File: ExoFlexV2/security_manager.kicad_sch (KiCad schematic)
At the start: 8 parts, among them U10 SN74HC7032D_V2, U6 SN74HC7032D_V2, U7 SN74HC7032D_V2, U8 SN74LV4T08PWR_V2, U9 SN74LV4T08PWR_V2

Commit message: quque truc
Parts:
- renumbered U9 to U10, U10 to U11, U6 to U7, U7 to U8, U8 to U9
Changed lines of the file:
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@@
   (symbol (lib_id "SymLib:SN74HC7032D_V2") (at 59.69 30.48 0) (unit 2)
     (in_bom yes) (on_board yes) (fields_autoplaced)
-    (property "Reference" "U6" (id 0) (at 59.69 21.59 0))
+    (property "Reference" "U7" (id 0) (at 59.69 21.59 0))
     (property "Value" "SN74HC7032D_V2" (id 1) (at 59.69 24.13 0))
     (property "Footprint" "FootPrint:SN74HC7032D" (id 2) (at 59.69 33.02 0)
@@
   (symbol (lib_id "SymLib:SN74HC7032D_V2") (at 148.59 81.28 0) (unit 3)
     (in_bom yes) (on_board yes) (fields_autoplaced)
-    (property "Reference" "U7" (id 0) (at 148.59 72.39 0))
+    (property "Reference" "U8" (id 0) (at 148.59 72.39 0))
     (property "Value" "SN74HC7032D_V2" (id 1) (at 148.59 74.93 0))
     (property "Footprint" "FootPrint:SN74HC7032D" (id 2) (at 148.59 83.82 0)
@@
   (symbol (lib_id "SymLib:SN74HC7032D_V2") (at 193.04 116.84 0) (unit 1)
     (in_bom yes) (on_board yes) (fields_autoplaced)
-    (property "Reference" "U10" (id 0) (at 193.04 107.95 0))
+    (property "Reference" "U11" (id 0) (at 193.04 107.95 0))
     (property "Value" "SN74HC7032D_V2" (id 1) (at 193.04 110.49 0))
     (property "Footprint" "FootPrint:SN74HC7032D" (id 2) (at 193.04 119.38 0)
@@
   (symbol (lib_id "SymLib:SN74LV4T08PWR_V2") (at 104.14 44.45 0) (unit 3)
     (in_bom yes) (on_board yes) (fields_autoplaced)
-    (property "Reference" "U8" (id 0) (at 104.14 35.56 0))
+    (property "Reference" "U9" (id 0) (at 104.14 35.56 0))
     (property "Value" "SN74LV4T08PWR_V2" (id 1) (at 104.14 38.1 0))
     (property "Footprint" "FootPrint:SN74LV4T08PWR" (id 2) (at 104.14 46.99 0)
@@
   (symbol (lib_id "power:+5V") (at 181.61 102.87 0) (unit 1)
     (in_bom yes) (on_board yes) (fields_autoplaced)
-    (property "Reference" "#PWR038" (id 0) (at 181.61 106.68 0)
+    (property "Reference" "#PWR042" (id 0) (at 181.61 106.68 0)
       (effects (font (size 1.27 1.27)) hide)
     )
@@
   (symbol (lib_id "power:GND") (at 204.47 123.19 0) (unit 1)
     (in_bom yes) (on_board yes) (fields_autoplaced)
-    (property "Reference" "#PWR039" (id 0) (at 204.47 129.54 0)
+    (property "Reference" "#PWR043" (id 0) (at 204.47 129.54 0)
       (effects (font (size 1.27 1.27)) hide)
     )
@@
   (symbol (lib_id "power:GND") (at 132.08 102.87 0) (unit 1)
     (in_bom yes) (on_board yes) (fields_autoplaced)
-    (property "Reference" "#PWR037" (id 0) (at 132.08 109.22 0)
+    (property "Reference" "#PWR041" (id 0) (at 132.08 109.22 0)
       (effects (font (size 1.27 1.27)) hide)
     )
@@
   (symbol (lib_id "power:+5V") (at 110.49 83.82 0) (unit 1)
     (in_bom yes) (on_board yes) (fields_autoplaced)
-    (property "Reference" "#PWR036" (id 0) (at 110.49 87.63 0)
+    (property "Reference" "#PWR040" (id 0) (at 110.49 87.63 0)
       (effects (font (size 1.27 1.27)) hide)
     )
@@
   (symbol (lib_id "power:GND") (at 87.63 83.82 0) (unit 1)
     (in_bom yes) (on_board yes) (fields_autoplaced)
-    (property "Reference" "#PWR035" (id 0) (at 87.63 90.17 0)
+    (property "Reference" "#PWR039" (id 0) (at 87.63 90.17 0)
       (effects (font (size 1.27 1.27)) hide)
     )
@@
   (symbol (lib_id "SymLib:SN74HC7032D_V2") (at 125.73 55.88 0) (unit 2)
     (in_bom yes) (on_board yes) (fields_autoplaced)
-    (property "Reference" "U7" (id 0) (at 125.73 46.99 0))
+    (property "Reference" "U8" (id 0) (at 125.73 46.99 0))
     (property "Value" "SN74HC7032D_V2" (id 1) (at 125.73 49.53 0))
     (property "Footprint" "FootPrint:SN74HC7032D" (id 2) (at 125.73 58.42 0)
@@
   (symbol (lib_id "SymLib:SN74LV4T08PWR_V2") (at 120.65 96.52 0) (unit 1)
     (in_bom yes) (on_board yes) (fields_autoplaced)
-    (property "Reference" "U9" (id 0) (at 120.65 87.63 0))
+    (property "Reference" "U10" (id 0) (at 120.65 87.63 0))
     (property "Value" "SN74LV4T08PWR_V2" (id 1) (at 120.65 90.17 0))
     (property "Footprint" "FootPrint:SN74LV4T08PWR" (id 2) (at 120.65 99.06 0)
@@
   (symbol (lib_id "SymLib:SN74HC7032D_V2") (at 81.28 55.88 0) (unit 4)
     (in_bom yes) (on_board yes) (fields_autoplaced)
-    (property "Reference" "U7" (id 0) (at 81.28 46.99 0))
+    (property "Reference" "U8" (id 0) (at 81.28 46.99 0))
     (property "Value" "SN74HC7032D_V2" (id 1) (at 81.28 49.53 0))
     (property "Footprint" "FootPrint:SN74HC7032D" (id 2) (at 81.28 58.42 0)
@@
   (symbol (lib_id "SymLib:SN74HC7032D_V2") (at 76.2 77.47 0) (unit 1)
     (in_bom yes) (on_board yes) (fields_autoplaced)
-    (property "Reference" "U7" (id 0) (at 76.2 68.58 0))
+    (property "Reference" "U8" (id 0) (at 76.2 68.58 0))
     (property "Value" "SN74HC7032D_V2" (id 1) (at 76.2 71.12 0))
     (property "Footprint" "FootPrint:SN74HC7032D" (id 2) (at 76.2 80.01 0)
@@
   (symbol (lib_id "SymLib:SN74HC7032D_V2") (at 81.28 35.56 0) (unit 3)
     (in_bom yes) (on_board yes) (fields_autoplaced)
-    (property "Reference" "U6" (id 0) (at 81.28 26.67 0))
+    (property "Reference" "U7" (id 0) (at 81.28 26.67 0))
     (property "Value" "SN74HC7032D_V2" (id 1) (at 81.28 29.21 0))
     (property "Footprint" "FootPrint:SN74HC7032D" (id 2) (at 81.28 38.1 0)
@@
   (symbol (lib_id "SymLib:SN74HC7032D_V2") (at 59.69 119.38 0) (unit 4)
     (in_bom yes) (on_board yes) (fields_autoplaced)
-    (property "Reference" "U6" (id 0) (at 59.69 110.49 0))
+    (property "Reference" "U7" (id 0) (at 59.69 110.49 0))
     (property "Value" "SN74HC7032D_V2" (id 1) (at 59.69 113.03 0))
     (property "Footprint" "FootPrint:SN74HC7032D" (id 2) (at 59.69 121.92 0)
@@
   (symbol (lib_id "SymLib:SN74LV4T08PWR_V2") (at 104.14 72.39 0) (unit 4)
     (in_bom yes) (on_board yes) (fields_autoplaced)
-    (property "Reference" "U8" (id 0) (at 104.14 63.5 0))
+    (property "Reference" "U9" (id 0) (at 104.14 63.5 0))
     (property "Value" "SN74LV4T08PWR_V2" (id 1) (at 104.14 66.04 0))
     (property "Footprint" "FootPrint:SN74LV4T08PWR" (id 2) (at 104.14 74.93 0)
@@
   (symbol (lib_id "power:+5V") (at 64.77 64.77 0) (unit 1)
     (in_bom yes) (on_board yes) (fields_autoplaced)
-    (property "Reference" "#PWR034" (id 0) (at 64.77 68.58 0)
-      (effects (font (size 1.27 1.27)) hide)
-    )
+    (property "Reference" "#PWR038" (id 0) (at 64.77 68.58 0)
+      (effects (font (size 1.27 1.27)) hide)
+    )

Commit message: Placement
Début du placement et modification d'après dernier review
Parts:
- added TP10, TP11, TP12, TP13, TP14, TP15, TP16, TP17, TP18, TP19: 5005, FootPrint:KEYSTONE_5005, symbol SymLib:5005
- renumbered U7 to U6, U11 to U6, U8 to U7, U9 to U8, U10 to U9
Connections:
- net at U6.6 (2Y), U6.9 (3A): now also TP10.TP
- net at U7.10 (3B), U9.3 (1Y): now also TP18.TP
- net at U6.1 (1A), U7.8 (3Y): now also TP19.TP
- net at U7.6 (2Y), U7.9 (3A): now also TP17.TP
- net at U6.11 (4Y), U6.2 (1B): now also TP11.TP
- net at U7.11 (4Y), U8.10 (3B), U8.12 (4A)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: now also TP14.TP
- net at U7.4 (2A), U8.8 (3Y): now also TP15.TP
- net at U6.8 (3Y), U8.9 (3A): now also TP12.TP
- net at U7.5 (2B), U8.11 (4Y): now also TP16.TP
- net at U7.3 (1Y), U8.13 (4B): now also TP13.TP

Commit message: Placement encore
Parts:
- renumbered C17 to C18, C18 to C19, C19 to C20, U9 to U10, U6 to U7, U7 to U8, U8 to U9
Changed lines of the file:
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@@
   (symbol (lib_id "Device:C") (at 102.87 88.9 0) (unit 1)
     (in_bom yes) (on_board yes)
-    (property "Reference" "C18" (id 0) (at 99.06 86.36 0)
+    (property "Reference" "C19" (id 0) (at 99.06 86.36 0)
       (effects (font (size 1.27 1.27)) (justify left))
     )
@@
   (symbol (lib_id "SymLib:SN74HC7032D_V2") (at 59.69 30.48 0) (unit 2)
     (in_bom yes) (on_board yes) (fields_autoplaced)
-    (property "Reference" "U6" (id 0) (at 59.69 21.59 0))
+    (property "Reference" "U7" (id 0) (at 59.69 21.59 0))
     (property "Value" "SN74HC7032D_V2" (id 1) (at 59.69 24.13 0))
     (property "Footprint" "FootPrint:SN74HC7032D" (id 2) (at 59.69 33.02 0)
@@
   (symbol (lib_id "Device:C") (at 57.15 69.85 0) (unit 1)
     (in_bom yes) (on_board yes)
-    (property "Reference" "C17" (id 0) (at 53.34 67.31 0)
+    (property "Reference" "C18" (id 0) (at 53.34 67.31 0)
       (effects (font (size 1.27 1.27)) (justify left))
     )
@@
   (symbol (lib_id "SymLib:SN74HC7032D_V2") (at 148.59 81.28 0) (unit 3)
     (in_bom yes) (on_board yes) (fields_autoplaced)
-    (property "Reference" "U7" (id 0) (at 148.59 72.39 0))
+    (property "Reference" "U8" (id 0) (at 148.59 72.39 0))
     (property "Value" "SN74HC7032D_V2" (id 1) (at 148.59 74.93 0))
     (property "Footprint" "FootPrint:SN74HC7032D" (id 2) (at 148.59 83.82 0)
@@
   (symbol (lib_id "SymLib:SN74HC7032D_V2") (at 193.04 116.84 0) (unit 1)
     (in_bom yes) (on_board yes) (fields_autoplaced)
-    (property "Reference" "U6" (id 0) (at 193.04 107.95 0))
+    (property "Reference" "U7" (id 0) (at 193.04 107.95 0))
     (property "Value" "SN74HC7032D_V2" (id 1) (at 193.04 110.49 0))
     (property "Footprint" "FootPrint:SN74HC7032D" (id 2) (at 193.04 119.38 0)
@@
   (symbol (lib_id "SymLib:SN74LV4T08PWR_V2") (at 104.14 44.45 0) (unit 3)
     (in_bom yes) (on_board yes) (fields_autoplaced)
-    (property "Reference" "U8" (id 0) (at 104.14 35.56 0))
+    (property "Reference" "U9" (id 0) (at 104.14 35.56 0))
     (property "Value" "SN74LV4T08PWR_V2" (id 1) (at 104.14 38.1 0))
     (property "Footprint" "FootPrint:SN74LV4T08PWR" (id 2) (at 104.14 46.99 0)
@@
   (symbol (lib_id "power:+5V") (at 181.61 102.87 0) (unit 1)
     (in_bom yes) (on_board yes) (fields_autoplaced)
-    (property "Reference" "#PWR049" (id 0) (at 181.61 106.68 0)
+    (property "Reference" "#PWR050" (id 0) (at 181.61 106.68 0)
       (effects (font (size 1.27 1.27)) hide)
     )
@@
   (symbol (lib_id "Device:C") (at 173.99 107.95 0) (unit 1)
     (in_bom yes) (on_board yes)
-    (property "Reference" "C19" (id 0) (at 170.18 105.41 0)
+    (property "Reference" "C20" (id 0) (at 170.18 105.41 0)
       (effects (font (size 1.27 1.27)) (justify left))
     )
@@
   (symbol (lib_id "power:GND") (at 204.47 123.19 0) (unit 1)
     (in_bom yes) (on_board yes) (fields_autoplaced)
-    (property "Reference" "#PWR050" (id 0) (at 204.47 129.54 0)
+    (property "Reference" "#PWR051" (id 0) (at 204.47 129.54 0)
       (effects (font (size 1.27 1.27)) hide)
     )
@@
   (symbol (lib_id "power:GND") (at 132.08 102.87 0) (unit 1)
     (in_bom yes) (on_board yes) (fields_autoplaced)
-    (property "Reference" "#PWR048" (id 0) (at 132.08 109.22 0)
+    (property "Reference" "#PWR049" (id 0) (at 132.08 109.22 0)
       (effects (font (size 1.27 1.27)) hide)
     )
@@
   (symbol (lib_id "power:+5V") (at 110.49 83.82 0) (unit 1)
     (in_bom yes) (on_board yes) (fields_autoplaced)
-    (property "Reference" "#PWR047" (id 0) (at 110.49 87.63 0)
+    (property "Reference" "#PWR048" (id 0) (at 110.49 87.63 0)
       (effects (font (size 1.27 1.27)) hide)
     )
@@
   (symbol (lib_id "power:GND") (at 87.63 83.82 0) (unit 1)
     (in_bom yes) (on_board yes) (fields_autoplaced)
-    (property "Reference" "#PWR046" (id 0) (at 87.63 90.17 0)
+    (property "Reference" "#PWR047" (id 0) (at 87.63 90.17 0)
       (effects (font (size 1.27 1.27)) hide)
     )
@@
   (symbol (lib_id "SymLib:SN74HC7032D_V2") (at 125.73 55.88 0) (unit 2)
     (in_bom yes) (on_board yes) (fields_autoplaced)
-    (property "Reference" "U7" (id 0) (at 125.73 46.99 0))
+    (property "Reference" "U8" (id 0) (at 125.73 46.99 0))
     (property "Value" "SN74HC7032D_V2" (id 1) (at 125.73 49.53 0))
     (property "Footprint" "FootPrint:SN74HC7032D" (id 2) (at 125.73 58.42 0)
@@
   (symbol (lib_id "SymLib:SN74LV4T08PWR_V2") (at 120.65 96.52 0) (unit 1)
     (in_bom yes) (on_board yes) (fields_autoplaced)
-    (property "Reference" "U9" (id 0) (at 120.65 87.63 0))
+    (property "Reference" "U10" (id 0) (at 120.65 87.63 0))
     (property "Value" "SN74LV4T08PWR_V2" (id 1) (at 120.65 90.17 0))
     (property "Footprint" "FootPrint:SN74LV4T08PWR" (id 2) (at 120.65 99.06 0)
@@
   (symbol (lib_id "SymLib:SN74HC7032D_V2") (at 81.28 55.88 0) (unit 4)
     (in_bom yes) (on_board yes) (fields_autoplaced)
-    (property "Reference" "U7" (id 0) (at 81.28 46.99 0))
+    (property "Reference" "U8" (id 0) (at 81.28 46.99 0))
     (property "Value" "SN74HC7032D_V2" (id 1) (at 81.28 49.53 0))
     (property "Footprint" "FootPrint:SN74HC7032D" (id 2) (at 81.28 58.42 0)
@@
   (symbol (lib_id "SymLib:SN74HC7032D_V2") (at 76.2 77.47 0) (unit 1)
     (in_bom yes) (on_board yes) (fields_autoplaced)
-    (property "Reference" "U7" (id 0) (at 76.2 68.58 0))
+    (property "Reference" "U8" (id 0) (at 76.2 68.58 0))
     (property "Value" "SN74HC7032D_V2" (id 1) (at 76.2 71.12 0))
     (property "Footprint" "FootPrint:SN74HC7032D" (id 2) (at 76.2 80.01 0)
@@
   (symbol (lib_id "SymLib:SN74HC7032D_V2") (at 81.28 35.56 0) (unit 3)
     (in_bom yes) (on_board yes) (fields_autoplaced)
-    (property "Reference" "U6" (id 0) (at 81.28 26.67 0))
+    (property "Reference" "U7" (id 0) (at 81.28 26.67 0))
     (property "Value" "SN74HC7032D_V2" (id 1) (at 81.28 29.21 0))
     (property "Footprint" "FootPrint:SN74HC7032D" (id 2) (at 81.28 38.1 0)
@@
   (symbol (lib_id "SymLib:SN74HC7032D_V2") (at 59.69 119.38 0) (unit 4)
     (in_bom yes) (on_board yes) (fields_autoplaced)
-    (property "Reference" "U6" (id 0) (at 59.69 110.49 0))
+    (property "Reference" "U7" (id 0) (at 59.69 110.49 0))
     (property "Value" "SN74HC7032D_V2" (id 1) (at 59.69 113.03 0))
     (property "Footprint" "FootPrint:SN74HC7032D" (id 2) (at 59.69 121.92 0)
@@
   (symbol (lib_id "SymLib:SN74LV4T08PWR_V2") (at 104.14 72.39 0) (unit 4)
     (in_bom yes) (on_board yes) (fields_autoplaced)
-    (property "Reference" "U8" (id 0) (at 104.14 63.5 0))
+    (property "Reference" "U9" (id 0) (at 104.14 63.5 0))
     (property "Value" "SN74LV4T08PWR_V2" (id 1) (at 104.14 66.04 0))
     (property "Footprint" "FootPrint:SN74LV4T08PWR" (id 2) (at 104.14 74.93 0)
@@
   (symbol (lib_id "power:+5V") (at 64.77 64.77 0) (unit 1)
     (in_bom yes) (on_board yes) (fields_autoplaced)
-    (property "Reference" "#PWR045" (id 0) (at 64.77 68.58 0)
-      (effects (font (size 1.27 1.27)) hide)
-    )
+    (property "Reference" "#PWR046" (id 0) (at 64.77 68.58 0)
+      (effects (font (size 1.27 1.27)) hide)
+    )

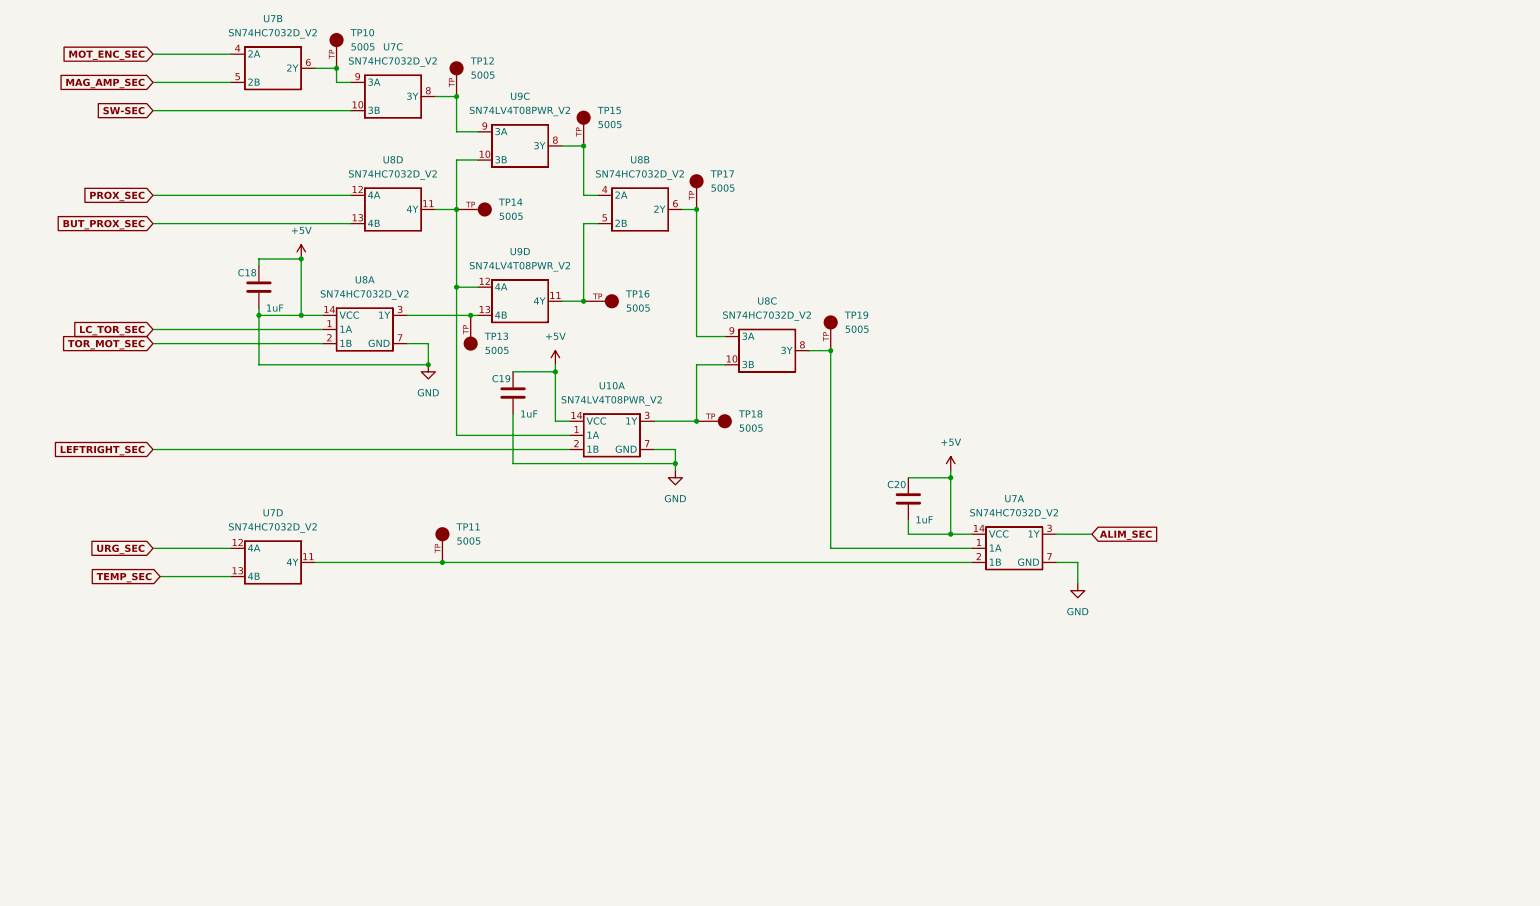
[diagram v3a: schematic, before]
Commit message: Mise à jour mi-stage
- Torque et Amplitude testé et vérifié
- Capteur de présence et de proximité testé
- Système de détection de coupure de fils
- Polyvalence pour plusieurs capteurs
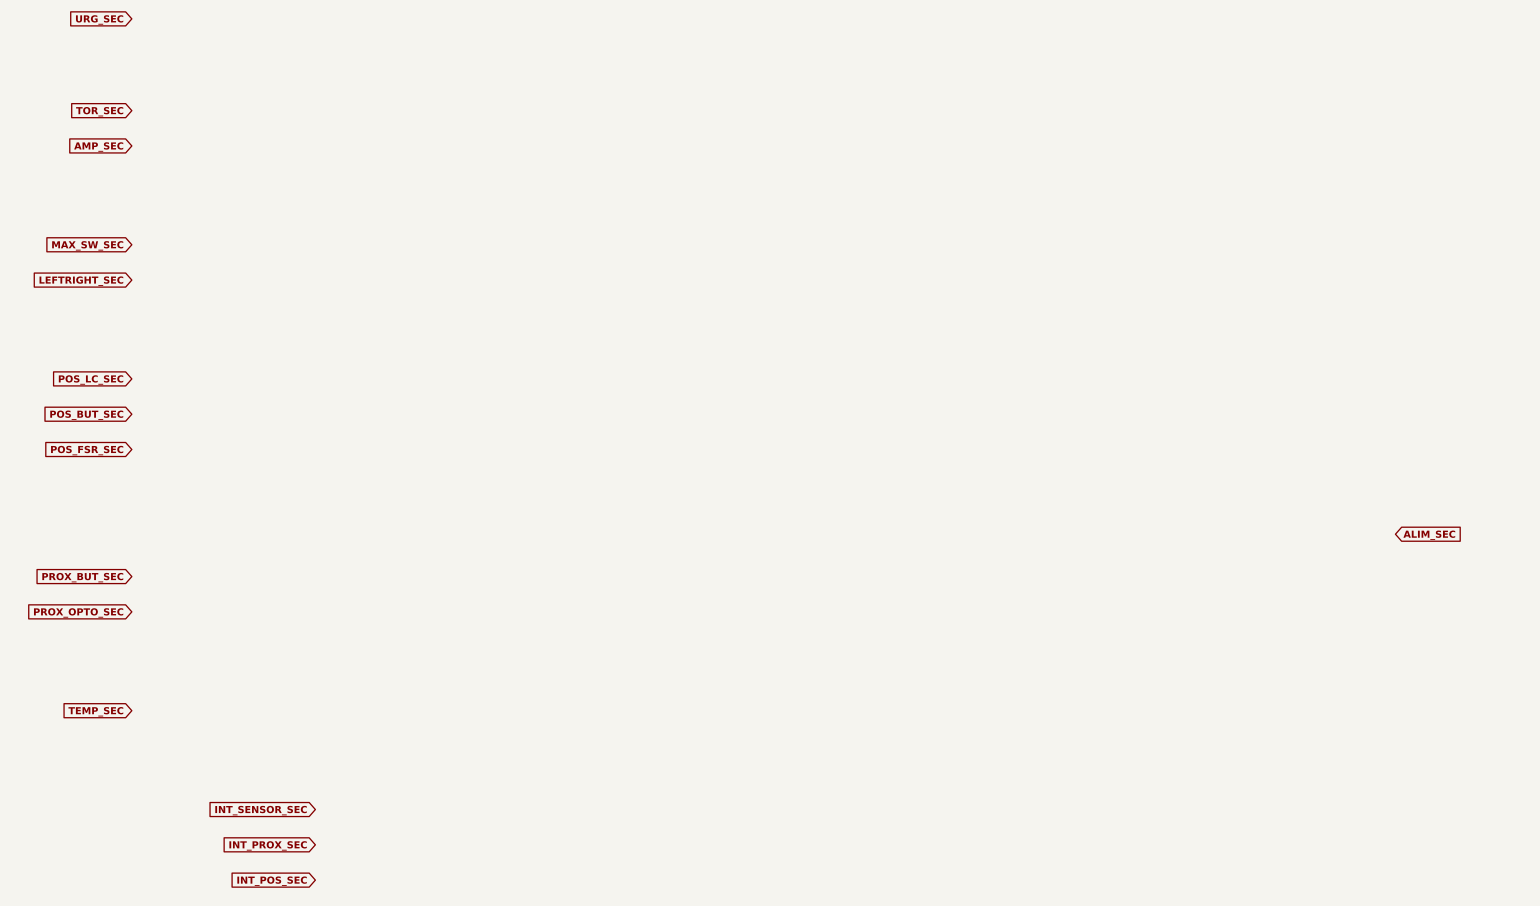
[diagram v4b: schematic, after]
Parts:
- removed C18, C19, C20: 1uF, Capacitor_SMD:C_0603_1608Metric, symbol Device:C
- removed TP10, TP11, TP12, TP13, TP14, TP15, TP16, TP17, TP18, TP19: 5005, FootPrint:KEYSTONE_5005, symbol SymLib:5005
- removed U10, U9: SN74LV4T08PWR_V2, FootPrint:SN74LV4T08PWR, symbol SymLib:SN74LV4T08PWR_V2
- removed U7, U8: SN74HC7032D_V2, FootPrint:SN74HC7032D, symbol SymLib:SN74HC7032D_V2
